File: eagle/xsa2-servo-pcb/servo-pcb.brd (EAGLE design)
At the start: 160 x 100 mm, 46 parts, among them IC1 ESP32-WROOM-32D__4MB_PS_, IC2 FT231XS-R, IC3 NJM2884U1-33-TE1, IC4 TPA2006D1DRBR, IC5 ISL90728UIE627Z-TK, J1 WJEK254-2.54-02P-140-00A, J3 WJEK254-2.54-02P-140-00A, J4 WJEK254-2.54-02P-140-00A, Q1 IRLML6402, Q2 2SC2712-GR_F_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

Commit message: [eagle] パターン追加
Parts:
- removed JP3: SERVO3, pinhead:1X03
- removed JP4: SERVO4, pinhead:1X03
- C5, C8: device rcl:C0603 -> rcl:C0805
- JP1, JP2: device pinhead:1X03 -> pinhead:2X03/90
- moved U$1 155.7 mm to (28.8, 34.6), turned to 180 degrees
- moved S2 142.5 mm to (17.8, 35.0)
- moved R18 140.5 mm to (13.2, 10.1), flipped to the bottom, turned to 180 degrees
- moved R17 140.1 mm to (12.8, 15.0), flipped to the bottom, turned to 270 degrees
- moved JP5 138.7 mm to (23.7, 29.9), turned to 180 degrees
- moved R16 133.1 mm to (14.5, 6.11), flipped to the bottom, turned to 270 degrees
- moved R15 130.3 mm to (12.5, 6.11), flipped to the bottom, turned to 270 degrees
- moved JP2 127.3 mm to (37.7, 28.6)
- moved JP1 112.9 mm to (37.7, 13.3), turned to 180 degrees
- moved R6 106.1 mm to (37.5, 29.8), flipped to the bottom, turned to 270 degrees
- moved R10 101.2 mm to (35.5, 36.3), flipped to the bottom, turned to 270 degrees
- moved R5 100.5 mm to (35.4, 29.7), flipped to the bottom, turned to 270 degrees
- moved C3 97.3 mm to (30.4, 37.6), flipped to the bottom
- moved R9 96.9 mm to (35.4, 33.1), flipped to the bottom, turned to 270 degrees
- moved R8 95.5 mm to (27.9, 10.1), flipped to the bottom, turned to 270 degrees
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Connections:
- net GND: now also JP1.5, JP1.6, JP2.5, JP2.6; no longer JP1.3, JP2.3, JP3.3, JP4.3
- net N$31: now also JP1.2; no longer JP2.1
- net N$32: now also JP2.1; no longer JP3.1
- net N$33: now also JP2.2; no longer JP4.1
- net VCC: now also U$1.B4,A9:VBUS
- net VDD: now also JP1.3, JP1.4, JP2.3, JP2.4; no longer JP1.2, JP2.2, JP3.2, JP4.2
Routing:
- net GND: track 0.00 -> 208.2 mm, vias 0 -> 7
- net VDD: track 0.00 -> 97.0 mm
- net +3V3: track 0.00 -> 94.6 mm, vias 0 -> 3
- net N$11: track 0.00 -> 81.4 mm, vias 0 -> 2
- net RXD: track 0.00 -> 76.4 mm, vias 0 -> 3
- net N$25: track 0.00 -> 71.7 mm, vias 0 -> 3
- net N$23: track 0.00 -> 62.9 mm, vias 0 -> 3
- net N$6: track 0.00 -> 55.1 mm, vias 0 -> 3
- net N$24: track 0.00 -> 51.0 mm, vias 0 -> 2
- net N$28: track 0.00 -> 46.0 mm, vias 0 -> 1
- net IO13: track 0.00 -> 37.8 mm, vias 0 -> 4
- net N$16: track 0.00 -> 36.7 mm, vias 0 -> 2
- net N$15: track 0.00 -> 36.0 mm, vias 0 -> 3
- net DTR: track 0.00 -> 33.2 mm
- net N$29: track 0.00 -> 31.0 mm, vias 0 -> 3
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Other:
- board size 160 x 100 mm -> 96 x 85 mm

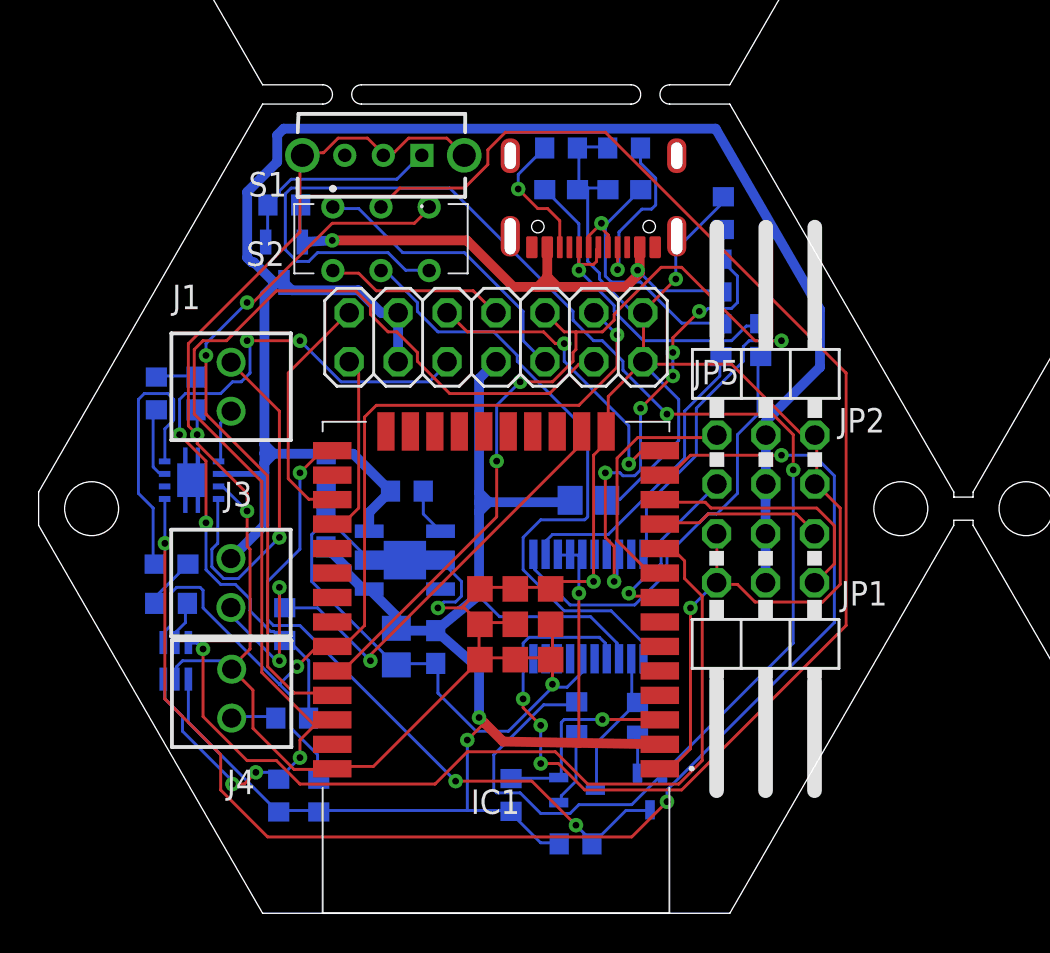
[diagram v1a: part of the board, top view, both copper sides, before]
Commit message: [eagle] メイン基板パターン設計完了
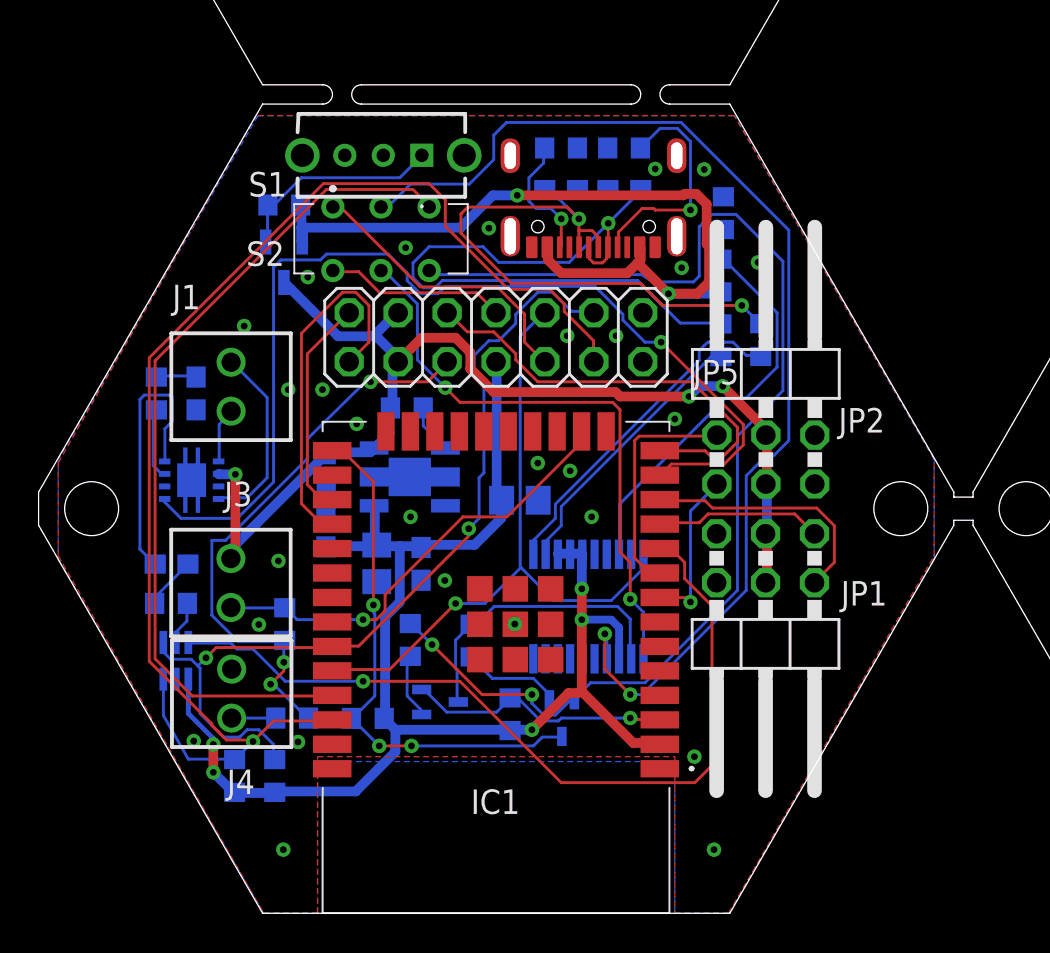
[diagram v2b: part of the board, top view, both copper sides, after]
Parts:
- moved R11 12.6 mm to (17.1, 10.1), turned to 180 degrees
- moved R7 9.54 mm to (22.4, 14.2)
- moved R8 9.54 mm to (19.3, 14.2)
- moved Q3 8.45 mm to (20.8, 11.0)
- moved Q2 5.95 mm to (27.2, 10.1)
- moved C8 4.44 mm to (17.5, 18.2)
- moved C9 4.38 mm to (19.8, 18.1)
- moved IC3 4.33 mm to (19.3, 22.6)
- moved R2 4.32 mm to (19.1, 26.2)
- moved R12 4.19 mm to (24.5, 10.3)
- moved C5 3.56 mm to (25.0, 21.4)
- moved R15 2.50 mm to (10.2, 7.13)
- moved R16 2.50 mm to (12.3, 7.13)
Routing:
- net GND: track 208.2 -> 0.00 mm, vias 7 -> 27
- net VDD: track 97.0 -> 60.6 mm, vias 0 -> 3
- net N$6: track 55.1 -> 34.4 mm, vias 3 -> 1
- net N$5: track 15.5 -> 35.7 mm
- net +3V3: track 94.6 -> 75.4 mm, vias 3 -> 5
- net N$11: track 81.4 -> 62.5 mm
- net N$25: track 71.7 -> 53.2 mm, vias 3 -> 1
- net RXD: track 76.4 -> 59.2 mm, vias 3 -> 2
- net VCC: track 29.6 -> 42.1 mm
- net N$1: track 19.4 -> 30.6 mm, vias 1 -> 2
- net N$4: track 9.55 -> 18.9 mm
- net N$26: track 18.4 -> 9.78 mm, vias 1 -> 0
- net N$15: track 36.0 -> 27.4 mm
- net IO13: track 37.8 -> 30.2 mm, vias 4 -> 3
- net N$29: track 31.0 -> 23.4 mm, vias 3 -> 1
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- added copper zone on layer 1, net GND
- added copper zone on layer 16, net GND
